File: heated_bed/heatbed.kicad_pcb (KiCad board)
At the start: 2 copper layers, 220 x 215 mm, 10 parts, among them P1 CONN_4

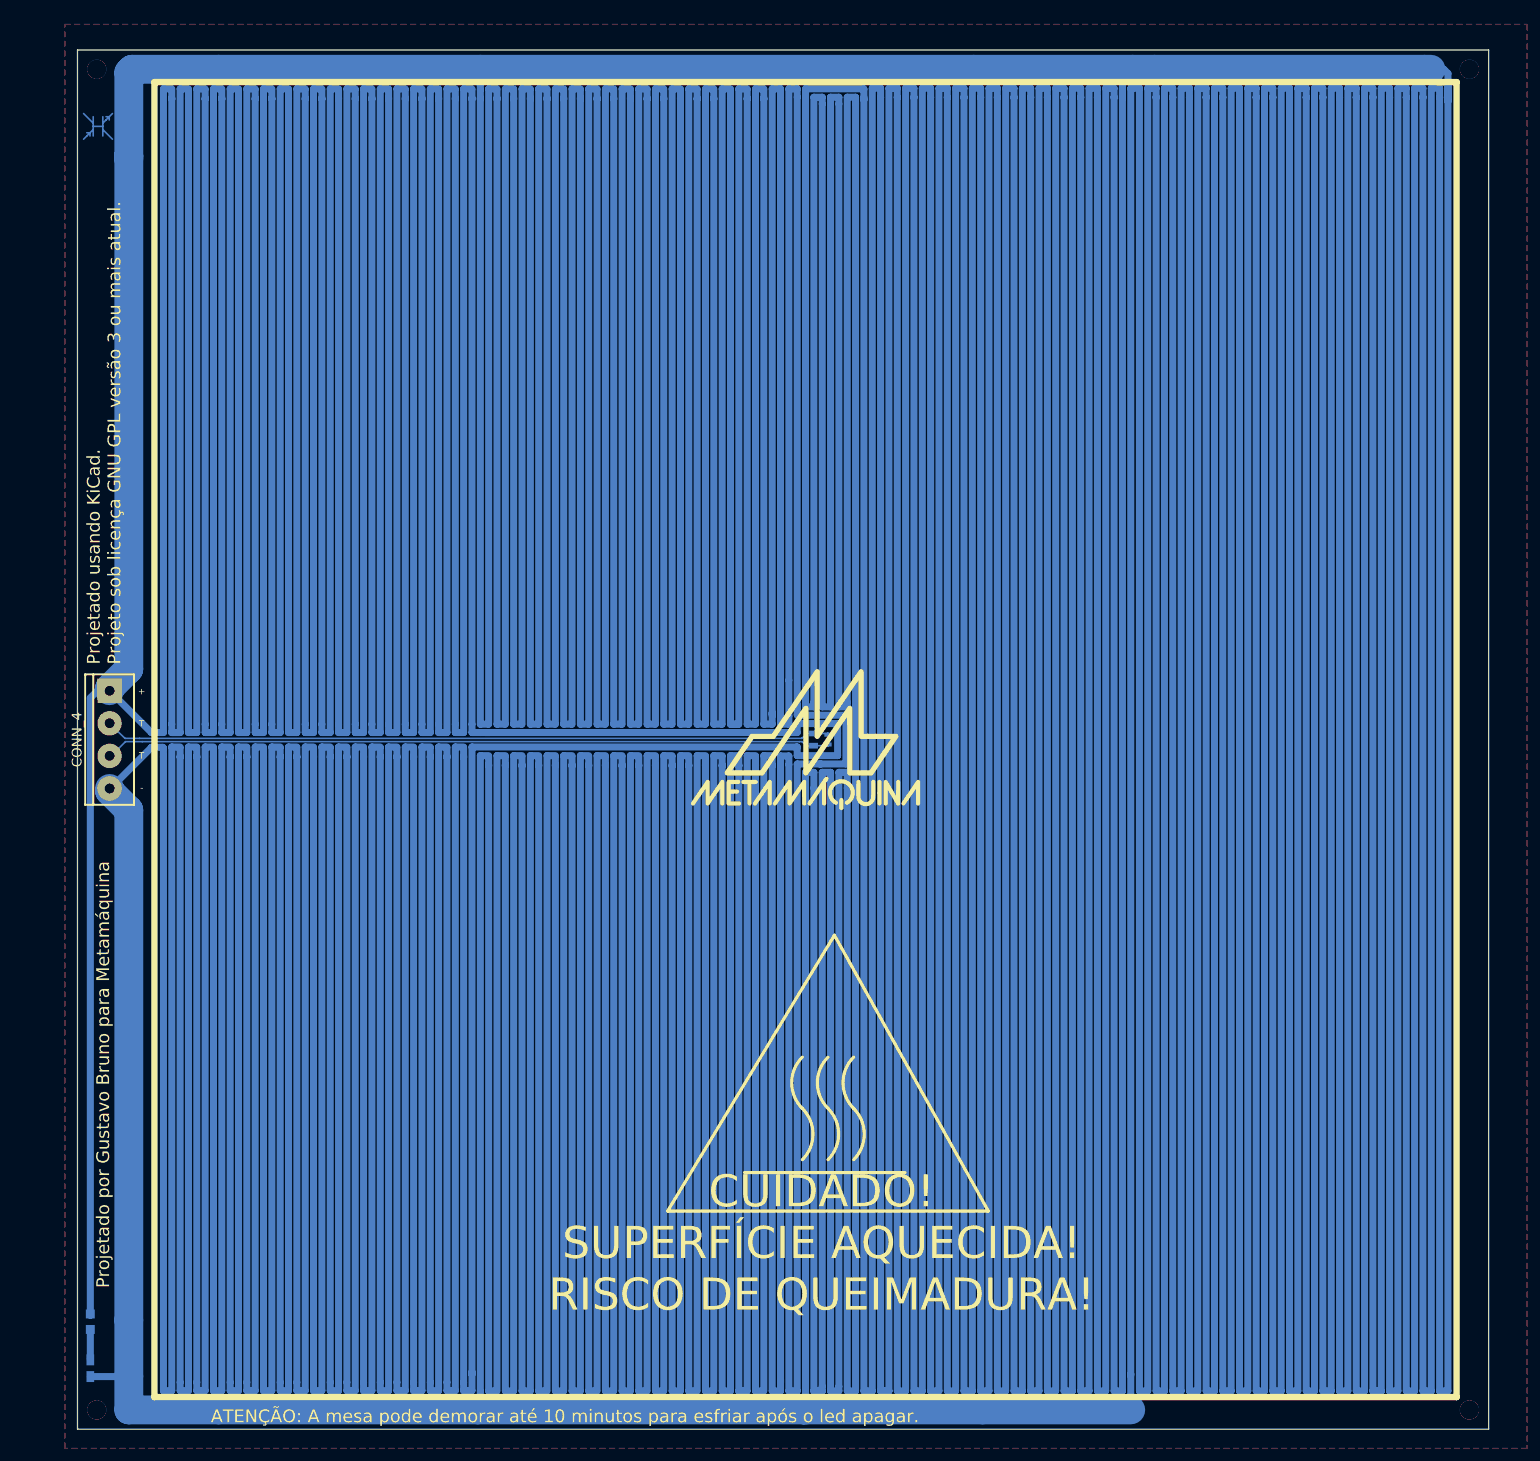
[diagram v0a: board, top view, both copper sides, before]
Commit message: Aumentada a placa para evitar colisao com extrusor
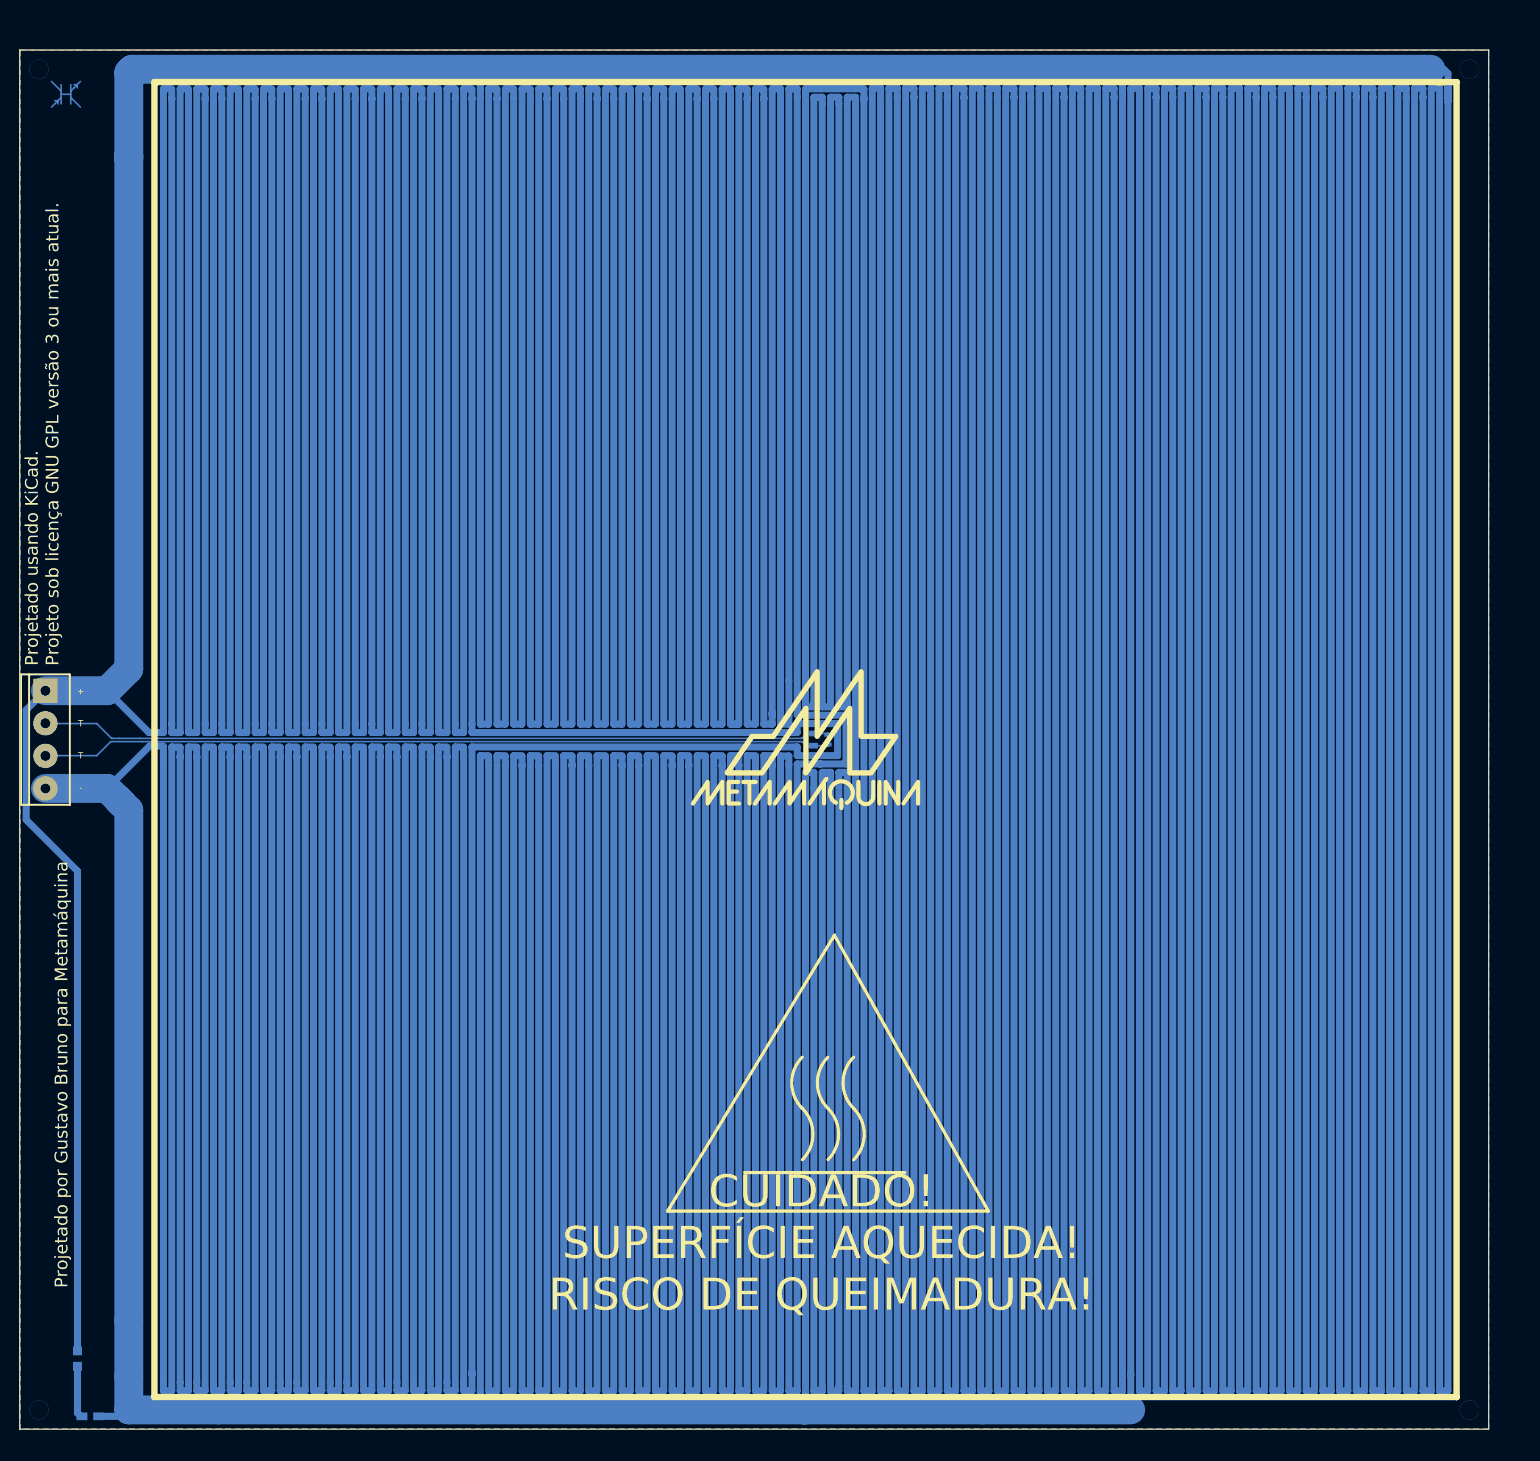
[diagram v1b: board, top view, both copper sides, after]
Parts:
- moved P1 10.0 mm to (19.0, 125.5)
- moved MH1 9.00 mm to (18.0, 21.0)
- moved MH4 9.00 mm to (18.0, 230.0)
- moved D1 7.50 mm to (26.0, 231.0), turned to 0 degrees
- moved R1 6.09 mm to (24.0, 222.0)
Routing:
- net N-000005: track 32310.7 -> 32334.4 mm
- net N-000001: track 114.1 -> 124.2 mm
- net N-000002: track 114.3 -> 124.3 mm
- net N-000003: track 4.74 -> 8.39 mm
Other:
- board size 220 x 215 mm -> 229 x 215 mm
- board text removed: "ATENÇÃO: A mesa pode demorar até 10 minutos para esfriar após o led apagar."

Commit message: Alteradas dimensoes para adequar ao vidro
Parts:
- moved R1 292.8 mm to (302.0, 130.0)
- moved D1 291.7 mm to (304.0, 142.5), turned to 270 degrees
- moved MH4 74.6 mm to (89.5, 251.2)
- moved MH1 72.6 mm to (89.5, 33.8)
- moved MH3 66.0 mm to (303.5, 251.2)
- moved VAL 64.1 mm to (199.0, 143.5), turned to 90 degrees
- moved MH2 63.8 mm to (303.5, 33.8)
- moved P1 63.3 mm to (80.0, 142.5)
- moved TH1 63.3 mm to (199.8, 142.5)
- moved TH2 63.3 mm to (202.0, 142.5)
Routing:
- net N-000005: track 32334.4 -> 32472.0 mm
- net N-000003: track 8.39 -> 10.0 mm
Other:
- board size 229 x 215 mm -> 230 x 227 mm

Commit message: Feitas fresas e cantos arredondados
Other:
- board size 230 x 227 mm -> 249.6 x 227 mm
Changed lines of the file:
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@@
     (links 8)
     (no_connects 1)
-    (area 15 18 313.529762 313.025)
+    (area 53.199999 28 313.529762 257.000001)
     (thickness 1.6)
-    (drawings 33)
+    (drawings 40)
     (tracks 897)
     (zones 0)
@@
     (visible_elements 7FFFFFFF)
     (pcbplotparams
-      (layerselection 2097152)
+      (layerselection 284196865)
       (usegerberextensions false)
       (excludeedgelayer false)
@@
       (xy 14.478 -0.6096) (xy 14.48816 -0.54864) (xy 14.4907 -0.48768) (xy 14.4907 -0.48768)) (layer F.SilkS) (width 0.00254))
   )
-  (gr_line (start 305 29) (end 306 29) (angle 90) (layer Edge.Cuts) (width 0.15))
-  (gr_line (start 306 256) (end 305 256) (angle 90) (layer Edge.Cuts) (width 0.15))
-  (gr_line (start 306 250) (end 306 256) (angle 90) (layer Edge.Cuts) (width 0.15))
-  (gr_line (start 76 250) (end 76 256) (angle 90) (layer Edge.Cuts) (width 0.15))
-  (gr_line (start 76 29) (end 85 29) (angle 90) (layer Edge.Cuts) (width 0.15))
-  (gr_line (start 76 35) (end 76 29) (angle 90) (layer Edge.Cuts) (width 0.15))
-  (gr_line (start 306 29) (end 306 35) (angle 90) (layer Edge.Cuts) (width 0.15))
-  (gr_line (start 85 256) (end 76 256) (angle 90) (layer Edge.Cuts) (width 0.15))
+  (gr_line (start 308.25 251.25) (end 308.25 249.9) (angle 90) (layer Edge.Cuts) (width 0.15))
+  (gr_arc (start 303.5 251.25) (end 308.25 251.25) (angle 90) (layer Edge.Cuts) (width 0.15))
+  (gr_line (start 308.25 33.8) (end 308.25 35.2) (angle 90) (layer Edge.Cuts) (width 0.15))
+  (gr_arc (start 303.5 33.75) (end 303.55 29) (angle 90) (layer Edge.Cuts) (width 0.15))
+  (gr_arc (start 89.5 33.75) (end 84.75 33.75) (angle 90) (layer Edge.Cuts) (width 0.15))
+  (gr_line (start 76 152.6) (end 76 132.4) (angle 90) (layer Edge.Cuts) (width 0.15))
+  (gr_arc (start 89.5 251.25) (end 89.5 256) (angle 90) (layer Edge.Cuts) (width 0.15))
+  (gr_line (start 84.75 129.2) (end 84.75 33.8) (angle 90) (layer Edge.Cuts) (width 0.15))
+  (gr_arc (start 79.2 132.4) (end 79.2 129.2) (angle -90) (layer Edge.Cuts) (width 0.15))
+  (gr_line (start 79.15 129.2) (end 84.75 129.2) (angle 90) (layer Edge.Cuts) (width 0.15))
+  (gr_arc (start 53.275 110.45) (end 53.275 110.45) (angle -90) (layer Edge.Cuts) (width 0.15))
+  (gr_line (start 58.675 125.475) (end 58.675 124.275) (angle 90) (layer Edge.Cuts) (width 0.15))
+  (gr_line (start 79.2 155.8) (end 84.75 155.8) (angle 90) (layer Edge.Cuts) (width 0.15))
+  (gr_arc (start 79.2 152.6) (end 79.2 155.8) (angle 90) (layer Edge.Cuts) (width 0.15))
+  (gr_arc (start 76 153) (end 76 153) (angle -90) (layer Edge.Cuts) (width 0.15))
+  (gr_line (start 84.75 251.2) (end 84.75 155.8) (angle 90) (layer Edge.Cuts) (width 0.15))
   (gr_line (start 221 141) (end 264 117) (angle 90) (layer F.SilkS) (width 0.5))
   (gr_line (start 264 167) (end 221 141) (angle 90) (layer F.SilkS) (width 0.5))
@@
   (gr_line (start 98 42) (end 98 243) (angle 90) (layer F.SilkS) (width 1))
   (gr_line (start 299 42) (end 98 42) (angle 90) (layer F.SilkS) (width 1))
-  (gr_line (start 76 250) (end 76 35) (angle 90) (layer Edge.Cuts) (width 0.15))
-  (gr_line (start 305 256) (end 85 256) (angle 90) (layer Edge.Cuts) (width 0.15))
-  (gr_line (start 306 35) (end 306 250) (angle 90) (layer Edge.Cuts) (width 0.15))
-  (gr_line (start 85 29) (end 305 29) (angle 90) (layer Edge.Cuts) (width 0.15))
+  (gr_line (start 303.5 256) (end 89.5 256) (angle 90) (layer Edge.Cuts) (width 0.15))
+  (gr_line (start 308.25 35) (end 308.25 250) (angle 90) (layer Edge.Cuts) (width 0.15))
+  (gr_line (start 89.5 29) (end 303.5 29) (angle 90) (layer Edge.Cuts) (width 0.15))
   (segment (start 84.95 40.4) (end 84.95 40.9) (width 0.254) (layer B.Cu) (net 0))
   (segment (start 84.45 40.4) (end 84.95 40.4) (width 0.254) (layer B.Cu) (net 0))
@@
     (polygon
       (pts
-        (xy 307 257) (xy 75 257) (xy 75 28) (xy 307 28)
+        (xy 310 260) (xy 75 260) (xy 75 25) (xy 310 25)
       )
     )
